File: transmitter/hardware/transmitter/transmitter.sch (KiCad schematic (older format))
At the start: 27 parts, among them J1 SOIL, J2 SOIL, J3 USB_UART_OFF, J4 USB_UART_ON, J5 SOIL, J6 SOIL, J7 SOIL, J8 SOIL, J9 SOIL, SW1 SW_SPST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

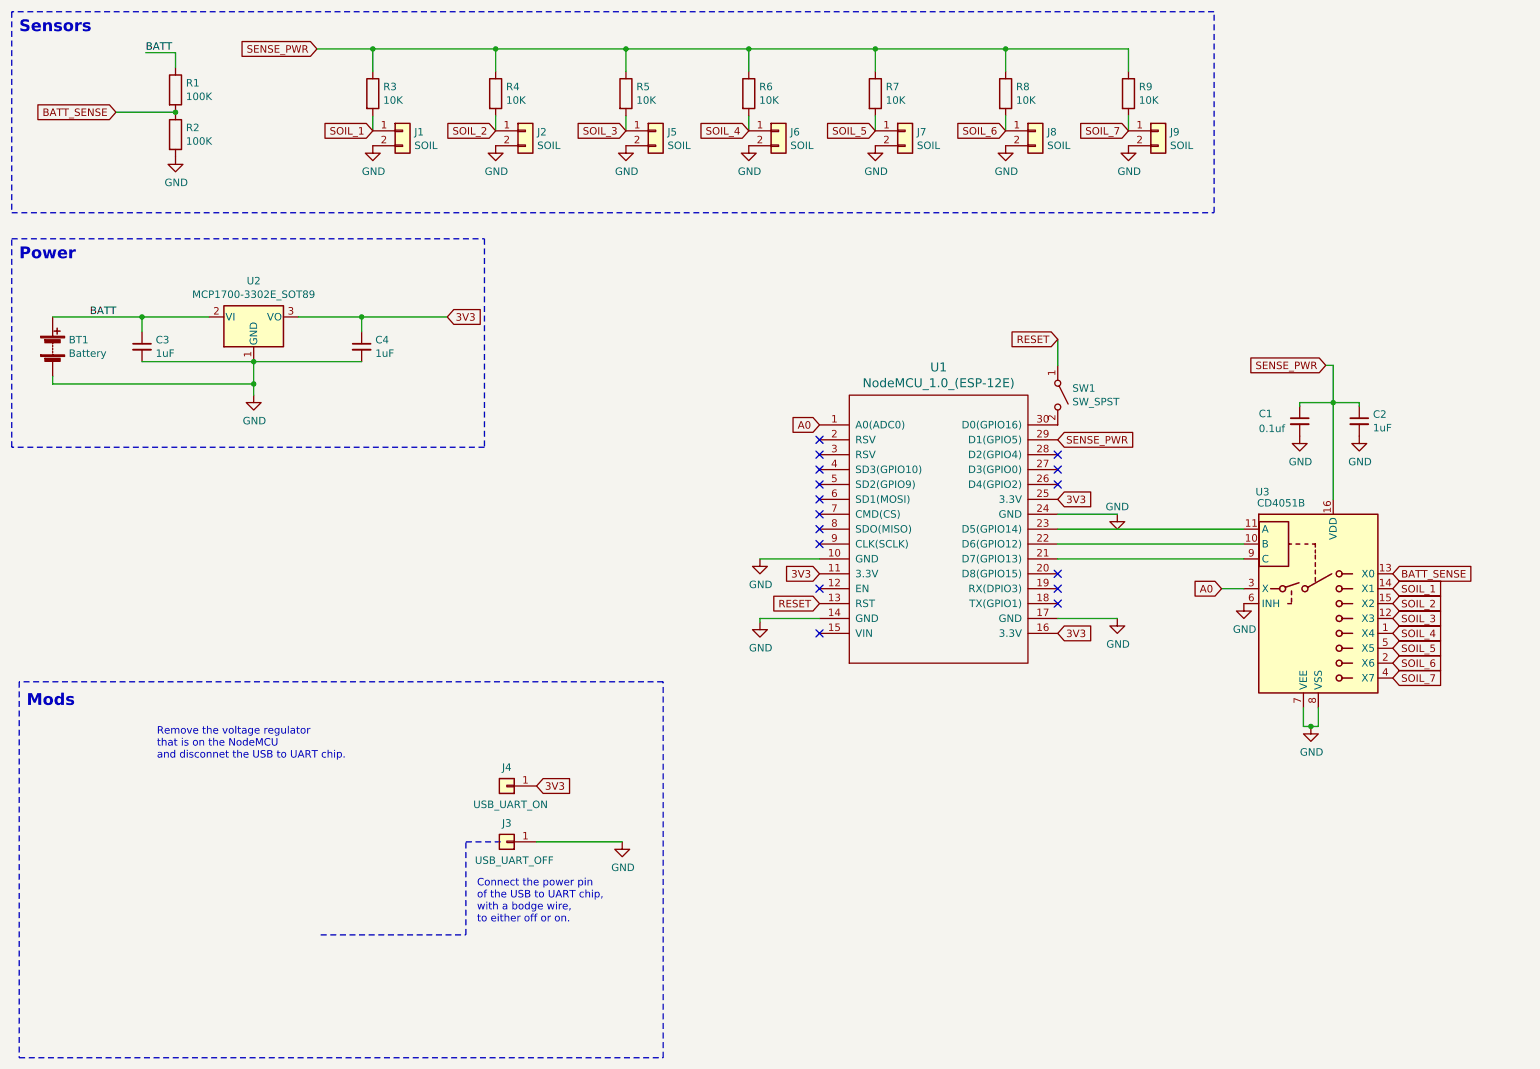
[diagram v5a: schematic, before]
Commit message: JST connectors
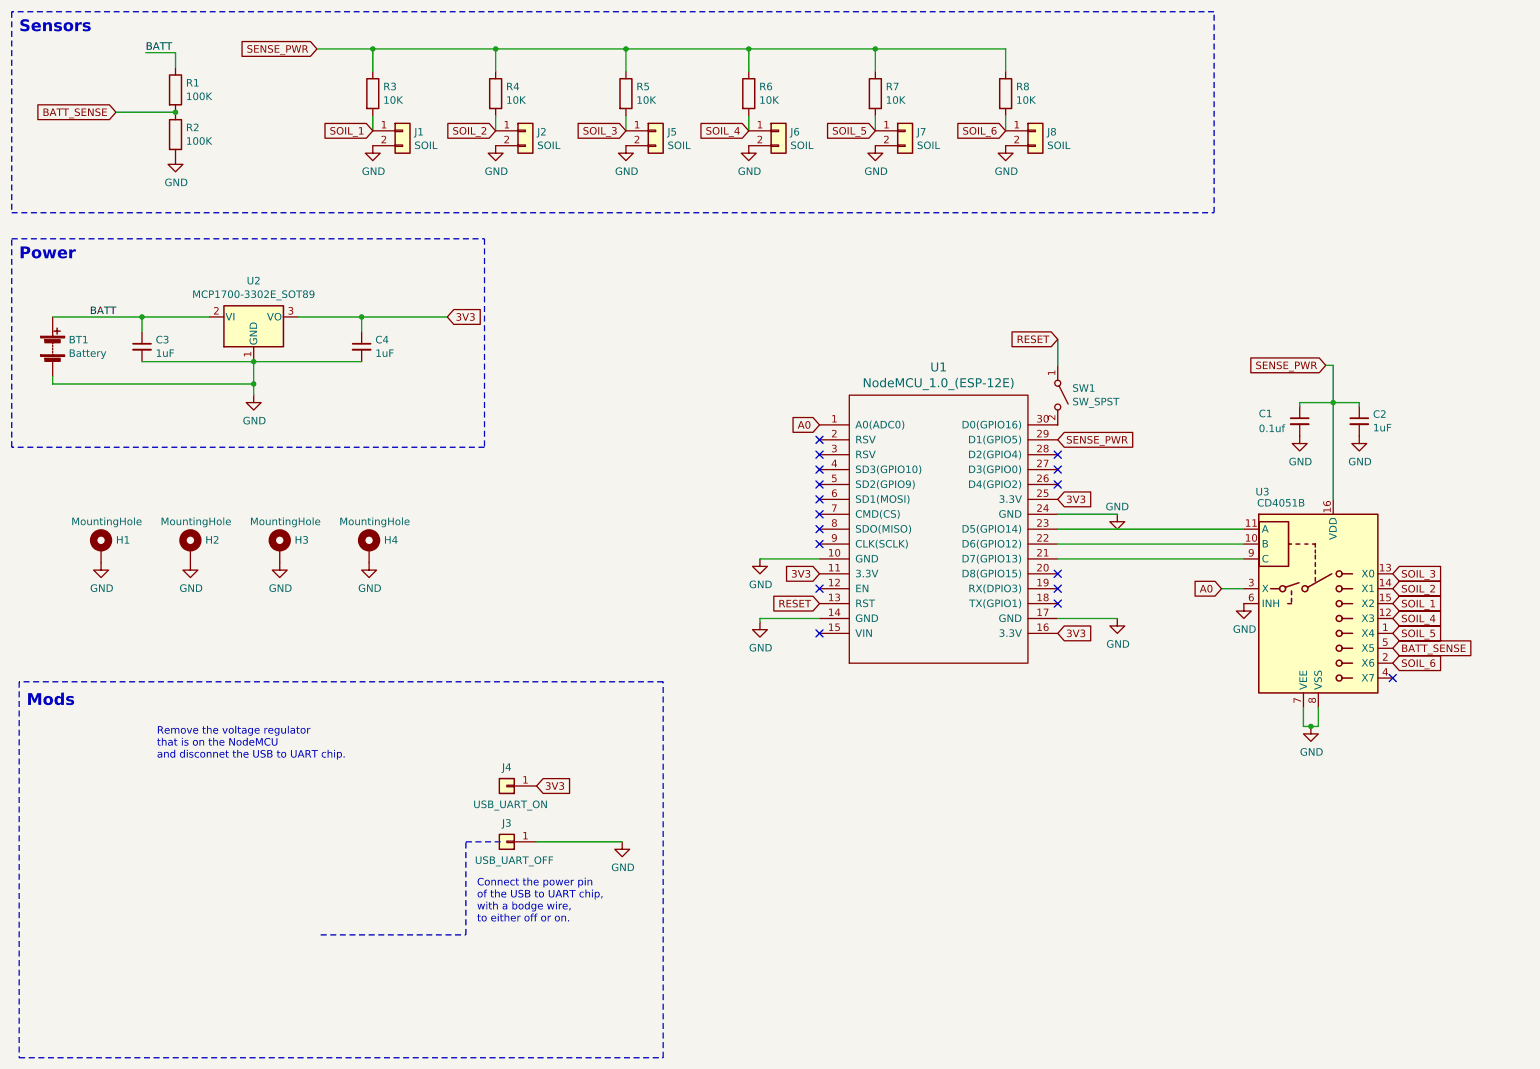
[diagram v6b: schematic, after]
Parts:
- removed J9: SOIL, Connector_PinHeader_2.54mm:PinHeader_1x02_P2.54mm_Vertical, symbol Connector_Generic:Conn_01x02
- removed R9: 10K, Resistor_SMD:R_0603_1608Metric_Pad1.05x0.95mm_HandSolder, symbol Device:R
- added H1, H2, H3, H4: MountingHole, MountingHole:MountingHole_3.2mm_M3_Pad, symbol Mechanical:MountingHole_Pad
- BT1, J1, J2, J5, J6, J7, J8: footprint Connector_PinHeader_2.54mm:PinHeader_1x02_P2.54mm_Vertical -> Connector_JST:JST_XH_B02B-XH-A_1x02_P2.50mm_Vertical
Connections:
- net BATT_SENSE: now also U3.5 (X5); no longer U3.13 (X0)
- net GND: now also H1.1, H2.1, H3.1, H4.1
- net SOIL_1: now also U3.15 (X2); no longer U3.14 (X1)
- net SOIL_2: now also U3.14 (X1); no longer U3.15 (X2)
- net SOIL_3: now also U3.13 (X0); no longer U3.12 (X3)
- net SOIL_4: now also U3.12 (X3); no longer U3.1 (X4)
- net SOIL_5: now also U3.1 (X4); no longer U3.5 (X5)
- net SOIL_7: no longer names the net of U3.4 (X7)
- no-connect marks 16 -> 17
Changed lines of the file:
@@
 F 0 "BT1" H 983 2846 50  0000 L CNN
 F 1 "Battery" H 983 2755 50  0000 L CNN
-F 2 "Connector_PinHeader_2.54mm:PinHeader_1x02_P2.54mm_Vertical" V 875 2860 50  0001 C CNN
+F 2 "Connector_JST:JST_XH_B02B-XH-A_1x02_P2.50mm_Vertical" V 875 2860 50  0001 C CNN
 F 3 "~" V 875 2860 50  0001 C CNN
 	1    875  2800
@@
 Text GLabel 1300 1225 0    50   Input ~ 0
 BATT_SENSE
-Text GLabel 9875 4325 2    50   Input ~ 0
+Text GLabel 9875 4825 2    50   Input ~ 0
 BATT_SENSE
 $Comp
@@
 F 0 "J1" H 3304 1342 50  0000 L CNN
 F 1 "SOIL" H 3304 1251 50  0000 L CNN
-F 2 "Connector_PinHeader_2.54mm:PinHeader_1x02_P2.54mm_Vertical" H 3225 1350 50  0001 C CNN
+F 2 "Connector_JST:JST_XH_B02B-XH-A_1x02_P2.50mm_Vertical" H 3225 1350 50  0001 C CNN
 F 3 "~" H 3225 1350 50  0001 C CNN
 	1    3225 1350
@@
 Text GLabel 7625 3825 2    50   Input ~ 0
 3V3
-Text GLabel 9875 4425 2    50   Input ~ 0
+Text GLabel 9875 4525 2    50   Input ~ 0
 SOIL_1
 $Comp
@@
 F 0 "J2" H 4129 1342 50  0000 L CNN
 F 1 "SOIL" H 4129 1251 50  0000 L CNN
-F 2 "Connector_PinHeader_2.54mm:PinHeader_1x02_P2.54mm_Vertical" H 4050 1350 50  0001 C CNN
+F 2 "Connector_JST:JST_XH_B02B-XH-A_1x02_P2.50mm_Vertical" H 4050 1350 50  0001 C CNN
 F 3 "~" H 4050 1350 50  0001 C CNN
 	1    4050 1350
@@
 F 0 "J5" H 5004 1342 50  0000 L CNN
 F 1 "SOIL" H 5004 1251 50  0000 L CNN
-F 2 "Connector_PinHeader_2.54mm:PinHeader_1x02_P2.54mm_Vertical" H 4925 1350 50  0001 C CNN
+F 2 "Connector_JST:JST_XH_B02B-XH-A_1x02_P2.50mm_Vertical" H 4925 1350 50  0001 C CNN
 F 3 "~" H 4925 1350 50  0001 C CNN
 	1    4925 1350
@@
 F 0 "J6" H 5829 1342 50  0000 L CNN
 F 1 "SOIL" H 5829 1251 50  0000 L CNN
-F 2 "Connector_PinHeader_2.54mm:PinHeader_1x02_P2.54mm_Vertical" H 5750 1350 50  0001 C CNN
+F 2 "Connector_JST:JST_XH_B02B-XH-A_1x02_P2.50mm_Vertical" H 5750 1350 50  0001 C CNN
 F 3 "~" H 5750 1350 50  0001 C CNN
 	1    5750 1350
@@
 F 0 "J7" H 6679 1342 50  0000 L CNN
 F 1 "SOIL" H 6679 1251 50  0000 L CNN
-F 2 "Connector_PinHeader_2.54mm:PinHeader_1x02_P2.54mm_Vertical" H 6600 1350 50  0001 C CNN
+F 2 "Connector_JST:JST_XH_B02B-XH-A_1x02_P2.50mm_Vertical" H 6600 1350 50  0001 C CNN
 F 3 "~" H 6600 1350 50  0001 C CNN
 	1    6600 1350
@@
 F 0 "J8" H 7554 1342 50  0000 L CNN
 F 1 "SOIL" H 7554 1251 50  0000 L CNN
-F 2 "Connector_PinHeader_2.54mm:PinHeader_1x02_P2.54mm_Vertical" H 7475 1350 50  0001 C CNN
+F 2 "Connector_JST:JST_XH_B02B-XH-A_1x02_P2.50mm_Vertical" H 7475 1350 50  0001 C CNN
 F 3 "~" H 7475 1350 50  0001 C CNN
 	1    7475 1350
@@
 Text GLabel 7275 1350 0    50   Input ~ 0
 SOIL_6
-$Comp
-L Device:R R9
-U 1 1 5DBDBBBF
-P 8100 1100
-F 0 "R9" H 8170 1146 50  0000 L CNN
-F 1 "10K" H 8170 1055 50  0000 L CNN
-F 2 "Resistor_SMD:R_0603_1608Metric_Pad1.05x0.95mm_HandSolder" V 8030 1100 50  0001 C CNN
-F 3 "~" H 8100 1100 50  0001 C CNN
-	1    8100 1100
-	1    0    0    -1
-$EndComp
-$Comp
-L Connector_Generic:Conn_01x02 J9
-U 1 1 5DBDBBC5
-P 8300 1350
-F 0 "J9" H 8379 1342 50  0000 L CNN
-F 1 "SOIL" H 8379 1251 50  0000 L CNN
-F 2 "Connector_PinHeader_2.54mm:PinHeader_1x02_P2.54mm_Vertical" H 8300 1350 50  0001 C CNN
-F 3 "~" H 8300 1350 50  0001 C CNN
-	1    8300 1350
-	1    0    0    -1
-$EndComp
-Wire Wire Line
-	8100 800  8100 950
-Wire Wire Line
-	8100 1250 8100 1350
-$Comp
-L power:GND #PWR015
-U 1 1 5DBDBBCE
-P 8100 1450
-F 0 "#PWR015" H 8100 1200 50  0001 C CNN
-F 1 "GND" H 8105 1277 50  0000 C CNN
-F 2 "" H 8100 1450 50  0001 C CNN
-F 3 "" H 8100 1450 50  0001 C CNN
-	1    8100 1450
-	1    0    0    -1
-$EndComp
-Text GLabel 8100 1350 0    50   Input ~ 0
-SOIL_7
 Wire Notes Line
 	600  550  600  1900
@@
 	6400 800  7275 800
 Connection ~ 6400 800
-Wire Wire Line
-	7275 800  8100 800
-Connection ~ 7275 800
-Text GLabel 9875 4525 2    50   Input ~ 0
+Text GLabel 9875 4425 2    50   Input ~ 0
 SOIL_2
-Text GLabel 9875 4625 2    50   Input ~ 0
+Text GLabel 9875 4325 2    50   Input ~ 0
 SOIL_3
-Text GLabel 9875 4725 2    50   Input ~ 0
+Text GLabel 9875 4625 2    50   Input ~ 0
 SOIL_4
-Text GLabel 9875 4825 2    50   Input ~ 0
+Text GLabel 9875 4725 2    50   Input ~ 0
 SOIL_5
 Text GLabel 9875 4925 2    50   Input ~ 0
 SOIL_6
-Text GLabel 9875 5025 2    50   Input ~ 0
-SOIL_7
+$Comp
+L Mechanical:MountingHole_Pad H1
+U 1 1 5DBE4537
+P 1200 4150
+F 0 "H1" H 1300 4201 50  0000 L CNN
+F 1 "MountingHole" H 1000 4325 50  0000 L CNN
+F 2 "MountingHole:MountingHole_3.2mm_M3_Pad" H 1200 4150 50  0001 C CNN
+F 3 "~" H 1200 4150 50  0001 C CNN
+	1    1200 4150
+	1    0    0    -1
+$EndComp
+$Comp
+L power:GND #PWR016
+U 1 1 5DBE45D3
+P 1200 4250
+F 0 "#PWR016" H 1200 4000 50  0001 C CNN
+F 1 "GND" H 1205 4077 50  0000 C CNN
+F 2 "" H 1200 4250 50  0001 C CNN
+F 3 "" H 1200 4250 50  0001 C CNN
+	1    1200 4250
+	1    0    0    -1
+$EndComp
+$Comp
+L Mechanical:MountingHole_Pad H2
+U 1 1 5DBE47CF
+P 1800 4150
+F 0 "H2" H 1900 4201 50  0000 L CNN
+F 1 "MountingHole" H 1600 4325 50  0000 L CNN
+F 2 "MountingHole:MountingHole_3.2mm_M3_Pad" H 1800 4150 50  0001 C CNN
+F 3 "~" H 1800 4150 50  0001 C CNN
+	1    1800 4150
+	1    0    0    -1
+$EndComp
+$Comp
+L power:GND #PWR017
+U 1 1 5DBE47D5
+P 1800 4250
+F 0 "#PWR017" H 1800 4000 50  0001 C CNN
+F 1 "GND" H 1805 4077 50  0000 C CNN
+F 2 "" H 1800 4250 50  0001 C CNN
+F 3 "" H 1800 4250 50  0001 C CNN
+	1    1800 4250
+	1    0    0    -1
+$EndComp
+$Comp
+L Mechanical:MountingHole_Pad H3
+U 1 1 5DBE5750
+P 2400 4150
+F 0 "H3" H 2500 4201 50  0000 L CNN
+F 1 "MountingHole" H 2200 4325 50  0000 L CNN
+F 2 "MountingHole:MountingHole_3.2mm_M3_Pad" H 2400 4150 50  0001 C CNN
+F 3 "~" H 2400 4150 50  0001 C CNN
+	1    2400 4150
+	1    0    0    -1
+$EndComp
+$Comp
+L power:GND #PWR018
+U 1 1 5DBE5756
+P 2400 4250
+F 0 "#PWR018" H 2400 4000 50  0001 C CNN
+F 1 "GND" H 2405 4077 50  0000 C CNN
+F 2 "" H 2400 4250 50  0001 C CNN
+F 3 "" H 2400 4250 50  0001 C CNN
+	1    2400 4250
+	1    0    0    -1
+$EndComp
+$Comp
+L Mechanical:MountingHole_Pad H4
+U 1 1 5DBE575C
+P 3000 4150
+F 0 "H4" H 3100 4201 50  0000 L CNN
+F 1 "MountingHole" H 2800 4325 50  0000 L CNN
+F 2 "MountingHole:MountingHole_3.2mm_M3_Pad" H 3000 4150 50  0001 C CNN
+F 3 "~" H 3000 4150 50  0001 C CNN
+	1    3000 4150
+	1    0    0    -1
+$EndComp
+$Comp
+L power:GND #PWR019
+U 1 1 5DBE5762
+P 3000 4250
+F 0 "#PWR019" H 3000 4000 50  0001 C CNN
+F 1 "GND" H 3005 4077 50  0000 C CNN
+F 2 "" H 3000 4250 50  0001 C CNN
+F 3 "" H 3000 4250 50  0001 C CNN
+	1    3000 4250
+	1    0    0    -1
+$EndComp
+NoConn ~ 9875 5025
 $EndSCHEMATC
